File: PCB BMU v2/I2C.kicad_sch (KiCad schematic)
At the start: 42 parts, among them J1 RJ45_Shielded, J2 RJ45_Shielded, U4 TCA9517ADGK, U5 ISO1540DR, U6 TCA9535PWR

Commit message: update code
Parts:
- C21, C8, C9: footprint Capacitor_SMD:C_0805_2012Metric -> Capacitor_SMD:C_0402_1005Metric; LCSC (none) -> C307331
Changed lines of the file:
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@@
 			)
 		)
-		(property "Footprint" "Capacitor_SMD:C_0805_2012Metric"
+		(property "Footprint" "Capacitor_SMD:C_0402_1005Metric"
 			(at 27.94 127 0)
 			(effects
@@
 			)
 		)
+		(property "LCSC" "C307331"
+			(at 27.94 127 0)
+			(effects
+				(font
+					(size 1.27 1.27)
+				)
+				(hide yes)
+			)
+		)
 		(pin "1"
 		)
@@
 			)
 		)
-		(property "Footprint" "Capacitor_SMD:C_0805_2012Metric"
+		(property "Footprint" "Capacitor_SMD:C_0402_1005Metric"
 			(at 247.65 67.31 0)
 			(effects
@@
 			)
 		)
-		(property "Description" ""
+		(property "Description" "C307331"
+			(at 247.65 67.31 0)
+			(effects
+				(font
+					(size 1.27 1.27)
+				)
+				(hide yes)
+			)
+		)
+		(property "LCSC" "C307331"
 			(at 247.65 67.31 0)
 			(effects
@@
 			)
 		)
-		(property "Footprint" "Capacitor_SMD:C_0805_2012Metric"
+		(property "Footprint" "Capacitor_SMD:C_0402_1005Metric"
 			(at 264.16 67.31 0)
 			(effects
@@
 			(at 264.16 67.31 0)
 			(effects
+				(font
+					(size 1.27 1.27)
+				)
+				(hide yes)
+			)
+		)
+		(property "LCSC" "C307331"
+			(at 264.16 67.31 0)
+			(effects

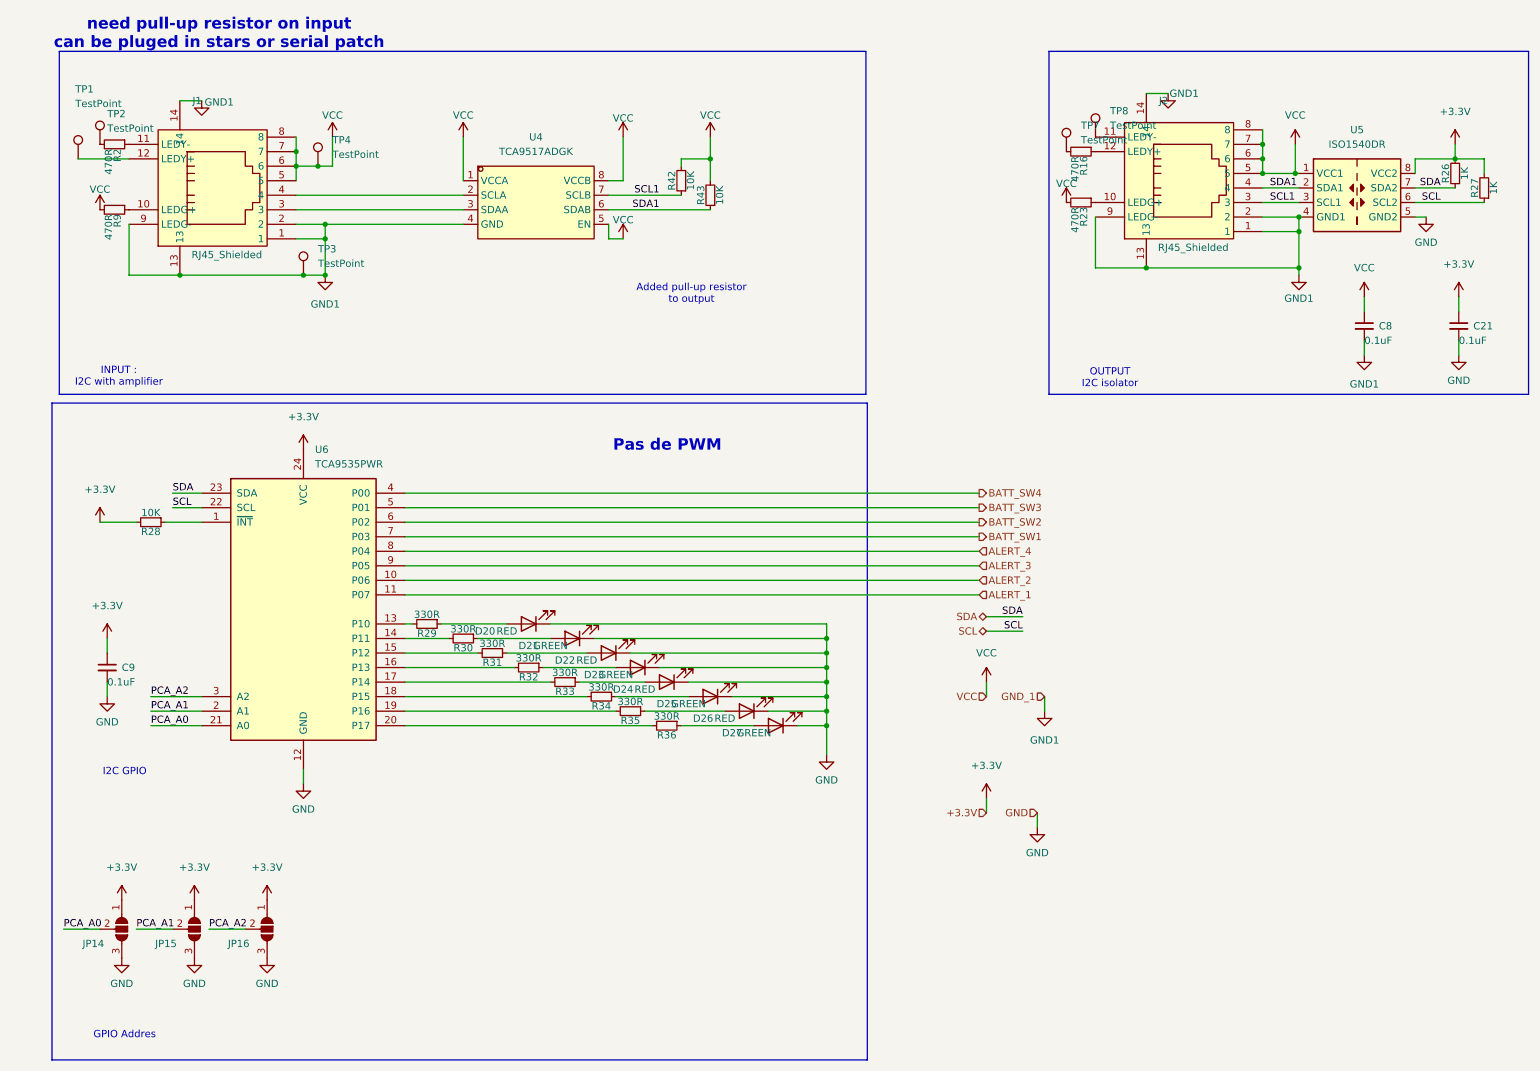
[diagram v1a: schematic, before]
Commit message: add Ampère/Houre calculation
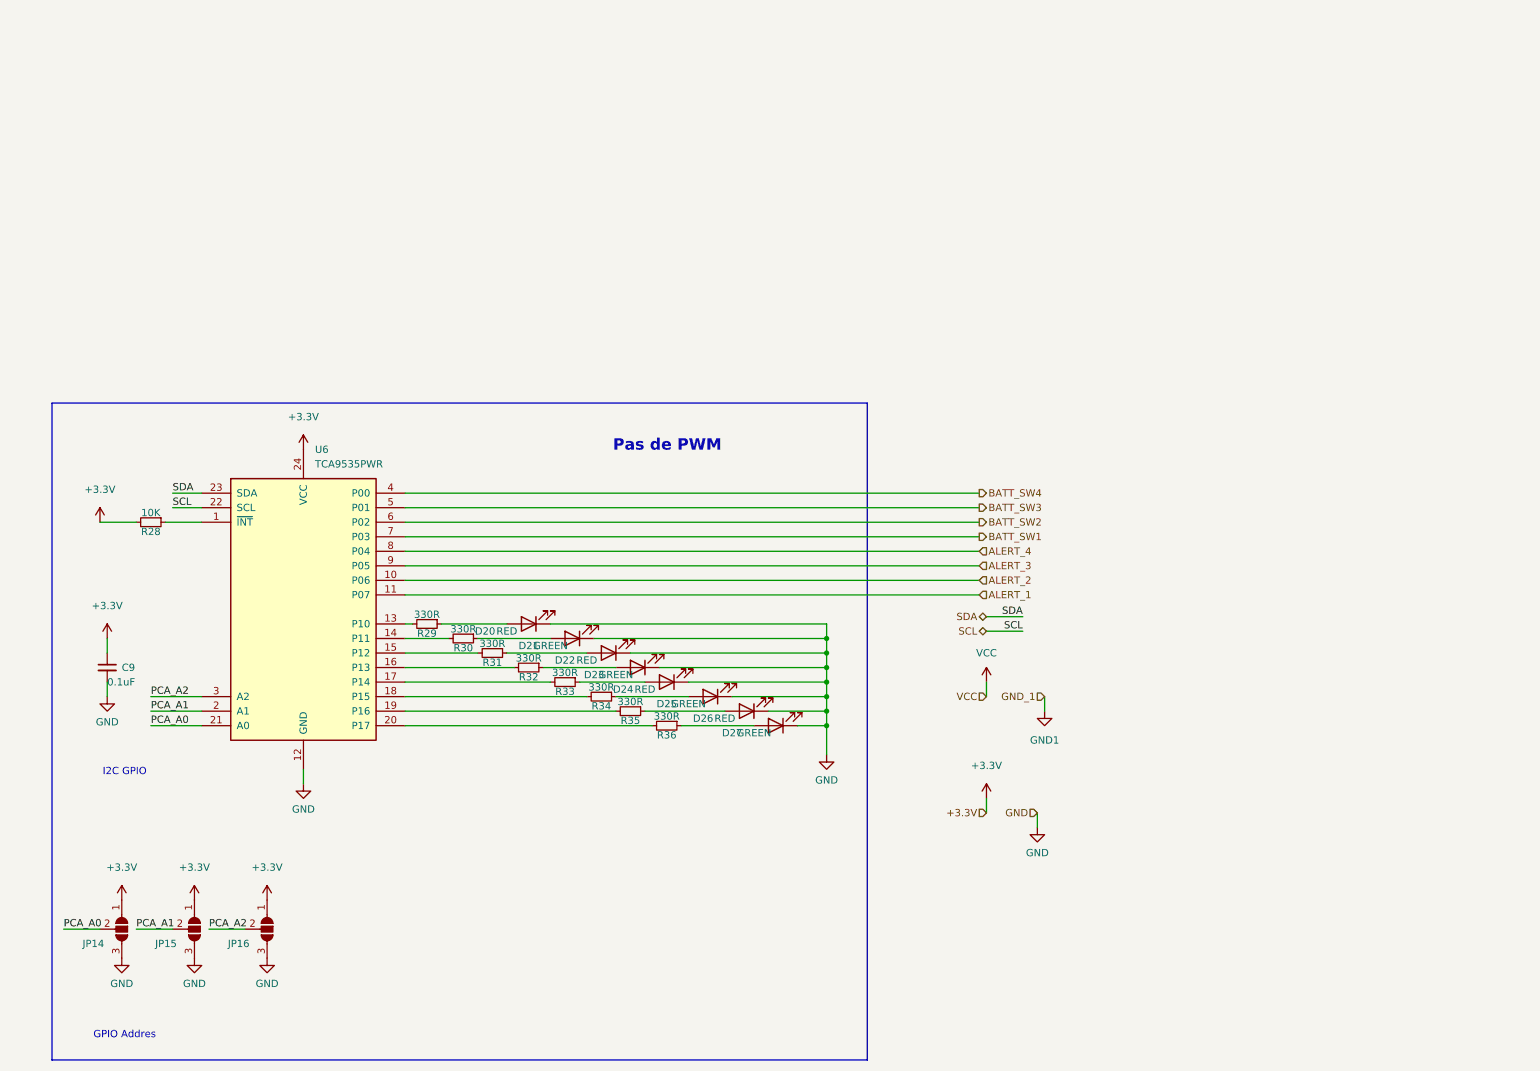
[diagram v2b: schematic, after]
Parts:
- removed C21, C8: 0.1uF, Capacitor_SMD:C_0402_1005Metric, symbol Device:C_Small
- removed J1, J2: RJ45_Shielded, easyeda2kicad:RJ45-TH_RC01061, symbol easyeda2kicad:RC01061
- removed R16, R2, R23, R9: 470R, Resistor_SMD:R_0603_1608Metric, symbol Device:R_Small
- removed R26, R27: 1K, Resistor_SMD:R_0603_1608Metric, symbol Device:R_Small
- removed R42, R43: 10K, Resistor_SMD:R_0603_1608Metric, symbol Device:R_Small
- removed TP1, TP2, TP3, TP4, TP7, TP8: TestPoint, symbol Connector:TestPoint
- removed U4: TCA9517ADGK, easyeda2kicad:VSSOP-8_L3.0-W3.0-P0.65-LS5.0-BL, symbol easyeda2kicad:TCA9517ADGKR
- removed U5: ISO1540DR, Package_SO:SOIC-8_3.9x4.9mm_P1.27mm, symbol Isolator:ISO1540
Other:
- note removed: "Added pull-up resistor to output"
- note removed: "INPUT : I2C with amplifier"
- note removed: "OUTPUT I2C isolator"
- note removed: "need pull-up resistor on input can be pluged in stars or serial patch"
